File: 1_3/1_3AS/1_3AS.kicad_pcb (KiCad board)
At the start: 2 copper layers, 118.5 x 93.4 mm, 45 parts, among them SW10 SW_SPST, SW11 SW_SPST, SW12 SW_SPST, SW14 SW_SPST, SW15 SW_SPST, SW16 SW_SPST, SW17 SW_SPST, SW18 SW_SPST, SW19 SW_SPST, SW2 SW_SPST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

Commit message: AS chk
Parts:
- moved H4 0.46 mm to (186.2, 116.0)

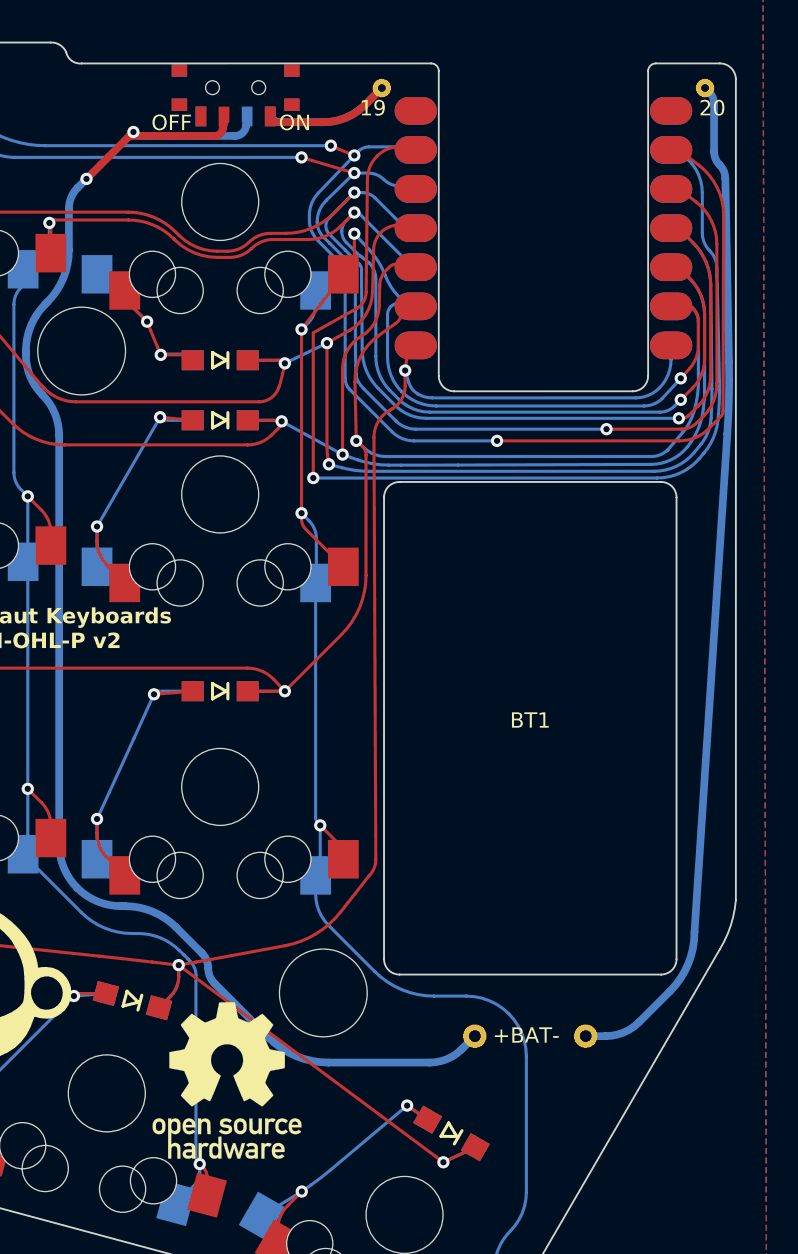
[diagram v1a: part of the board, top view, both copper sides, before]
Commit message: adjust d19,20,21 all
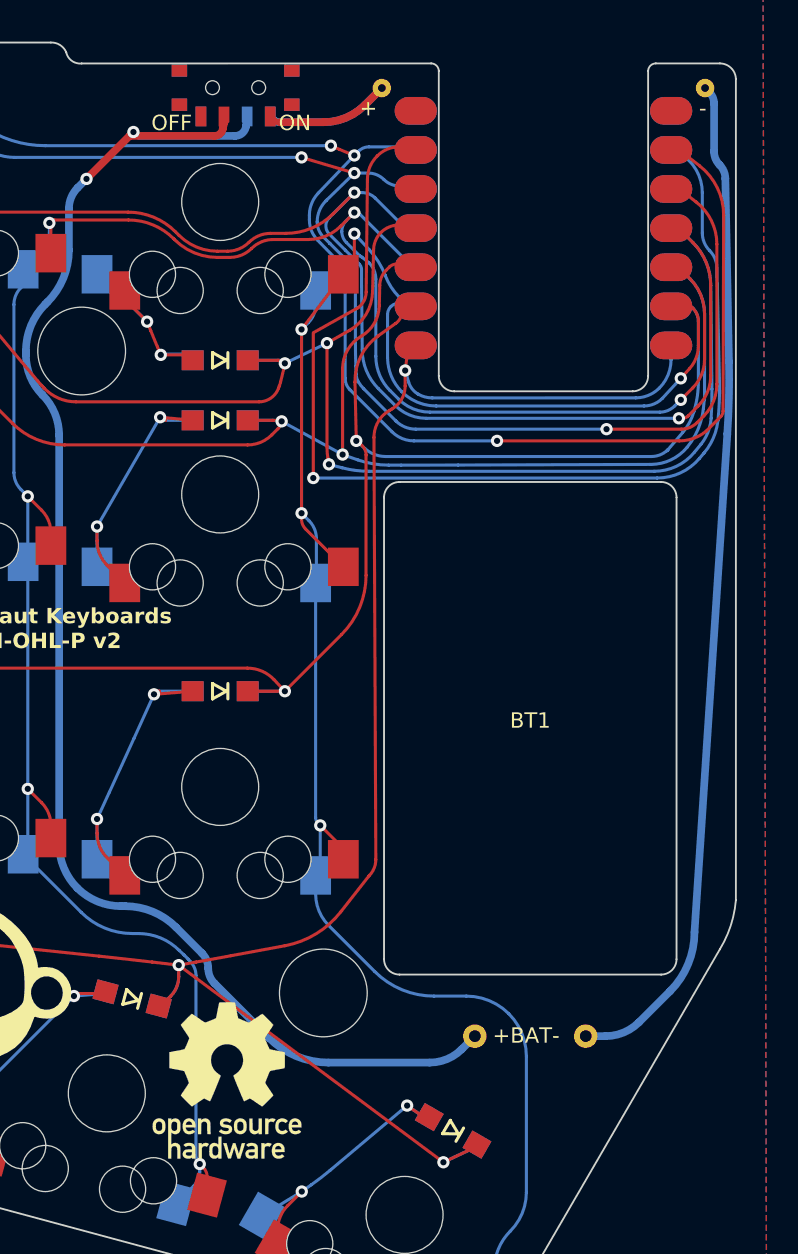
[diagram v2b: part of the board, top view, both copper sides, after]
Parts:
- moved D21 0.20 mm to (194.6, 125.0)
- moved D20 0.11 mm to (173.8, 116.4)
